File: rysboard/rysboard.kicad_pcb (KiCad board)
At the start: 4 copper layers, 56 x 65 mm, 151 parts, among them J1 RPi4, J10 ToF1, J11 ToF2, J12 ToF3, J13 ToF4, J15 ToF5, J16 ToF6, J19 Fan_Connector, J2 Motor L, J20 Power_SW, J22 CH1_T, J23 CH2_T, J3 Motor R, J4 Cell3, J5 Cell2, J6 Cell1, J7 Conn_01x02, J9 IMU, Q1 DMP3036SSD-13, Q13 SI7997DP-T1-GE3, Q14 DMP2075UFDB-7-alt, Q2 DMP2075UFDB, Q3 NST847BDP6T5G, Q4 NST847BDP6T5G, Q5 DMP3036SSD-13, Q6 Si7938DP-T1-GE3, Q7 NST847BDP6T5G, Q9 Si7938DP-T1-GE3, U1 L6470, U2 L6470, U3 ST1S10, U4 STM32G031K8Ux, U5 74HC2G00, U6 AP7381-33SA-7, U7 LM74700, U8 LM74700, U9 INA181

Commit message: Bom finished pcb cleanup started
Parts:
- removed D10, D11, D12: TESDU5V0, Diode_SMD:D_0603_1608Metric_Pad1.05x0.95mm_HandSolder
- removed D14, D3: TSZU52C10 RG, Diode_SMD:D_0603_1608Metric
- removed D16: PTVS30VS1UR,115, Diode_SMD:D_SOD-123
- removed D7: LED, LED_SMD:LED_0805_2012Metric
- removed Q13: SI7997DP-T1-GE3, Package_SO:PowerPAK_SO-8_Dual
- removed Q14: DMP2075UFDB-7-alt, SamacSys_Parts:DMP2075UFDB7
- removed U7, U8: LM74700, Package_TO_SOT_SMD:SOT-23-6
- added D4: SZ1SMA15CAT3G, Diode_SMD:D_SMA_Handsoldering, F.Cu at (183.7, 89.7)
- added IC1: LM74801QDRRRQ1, LM74801QDRRRQ1, F.Cu at (165.7, 86.6)
- added IC2: LM74801QDRRRQ1, LM74801QDRRRQ1, F.Cu at (181.9, 100.7)
- added Q10: AO3401A, Package_TO_SOT_SMD:SOT-23, F.Cu at (168.6, 104.5)
- added Q11: AO3401A, Package_TO_SOT_SMD:SOT-23, F.Cu at (156.8, 104.5)
- added R32: 100R, Resistor_SMD:R_0603_1608Metric, F.Cu at (187.2, 98.9)
- D13: value TSZU52C10 RG -> SZ1SMA15CAT3G; footprint Diode_SMD:D_0603_1608Metric -> Diode_SMD:D_SMA_Handsoldering
- F2: footprint Fuse:Fuse_2512_6332Metric -> Fuse:Fuse_1206_3216Metric
- J22, J23: footprint Connector_PinHeader_1.00mm:PinHeader_1x02_P1.00mm_Vertical -> Connector_PinHeader_1.27mm:PinHeader_1x02_P1.27mm_Vertical
- Q2: value DMP2075UFDB -> FDG6304P; footprint SamacSys_Parts:DMP2075UFDB7 -> SOT65P210X110-6N; moved to F.Cu
- R10: value 110KR -> 10KR
- R15: value 10KR -> 100R; moved to F.Cu
- R16: value 100R -> 110KR; moved to F.Cu
- R17: value 100R -> 10KR; moved to F.Cu
- R19: value 10K -> 100R; moved to F.Cu
- R22, R24: value 10KR -> 110KR
- R8: value 10k -> 110KR
- U3: footprint Package_SO:TI_SO-PowerPAD-8 -> Package_DFN_QFN:DFN-8-1EP_4x4mm_P0.8mm_EP2.3x3.24mm
- moved R16 88.2 mm to (171.3, 88.7), turned to 0 degrees
- moved Q4 87.8 mm to (180.0, 93.2)
- moved R23 83.0 mm to (171.3, 91.2), turned to 0 degrees
- moved R22 77.3 mm to (165.1, 97.3), turned to 0 degrees
- moved Q9 71.4 mm to (171.5, 84.0), turned to 270 degrees
- moved R15 68.4 mm to (164.8, 94.8), turned to 0 degrees
- moved R17 67.8 mm to (161.1, 97.3), turned to 0 degrees
- moved Q2 65.0 mm to (156.9, 95.8)
- moved R19 56.9 mm to (168.8, 94.8), turned to 0 degrees
- moved C18 0.48 mm to (94.9, 107.9)
- moved R14 0.46 mm to (94.9, 111.0)
- moved U3 0.42 mm to (99.3, 109.6)
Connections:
- C28 pad 1: /Power Supply/Battery_Balancing/V_BAT_AF_PROT- -> Net-(C28-Pad1)
- C28 pad 2: Net-(C28-Pad2) -> +BATT
- C29 pad 2: +BATT -> +12V
- C31 pad 1: /Power Supply/Batterry_Charging_Powes_Spply/VCAP -> +BATT
- C31 pad 2: GND -> Net-(C31-Pad2)
- F1 pad 1: Net-(D10-Pad1) -> Net-(F1-Pad1)
- J20 pad 1: Net-(J20-Pad1) -> /Power Supply/Battery_Balancing/V_BAT_AF_PROT-
- J20 pad 2: /Power Supply/Battery_Balancing/V_BAT_AF_PROT+ -> Net-(F1-Pad1)
- J4 pad 1: Net-(D12-Pad2) -> Net-(F1-Pad2)
- J6 pad 2: Net-(F1-Pad2) -> /Power Supply/Battery_Balancing/V_BAT_AF_PROT+
- Q1 pad 3: +BATT -> (no net)
- Q1 pad 4: Net-(D3-Pad2) -> (no net)
- Q1 pad 5: +12V -> (no net)
- Q1 pad 6: +12V -> (no net)
- Q2 pad 1: MCU_3.3V -> Net-(Q2-Pad1)
- Q2 pad 3: /Sensors/TOF_5V -> Net-(J4-Pad2)
- Q2 pad 4: +5V -> Net-(Q2-Pad4)
- Q2 pad 6: MCU_ANALOG_SENSOR_V -> Net-(J5-Pad2)
- Q4 pad 1: GND -> (no net)
- Q4 pad 2: Net-(Q4-Pad2) -> (no net)
- Q4 pad 6: Net-(D3-Pad2) -> (no net)
- Q7 pad 3: Net-(Q2-Pad5) -> Net-(Q11-Pad1)
- Q9 pad 1: /Power Supply/Battery_Balancing/V_BAT_AF_PROT- -> +12V
- Q9 pad 2: Net-(Q9-Pad2) -> Net-(IC1-Pad8)
- Q9 pad 5: Net-(D12-Pad2) -> +BATT
- R1 pad 1: +3V3 -> GND
- R10 pad 1: +BATT -> Net-(Q2-Pad2)
- R10 pad 2: Net-(D3-Pad2) -> /Power Supply/Battery_Balancing/V_BAT_AF_PROT-
- R15 pad 1: Net-(Q9-Pad2) -> Net-(Q2-Pad4)
- R15 pad 2: Net-(D11-Pad2) -> V_CELL1
- R16 pad 1: Net-(J5-Pad2) -> Net-(Q2-Pad5)
- R16 pad 2: Net-(D10-Pad2) -> Net-(J4-Pad2)
- R17 pad 1: Net-(J4-Pad2) -> Net-(Q2-Pad5)
- R17 pad 2: Net-(D11-Pad2) -> /Power Supply/Battery_Balancing/V_BAT_AF_PROT-
- R18 pad 1: Net-(J20-Pad1) -> Net-(IC1-Pad4)
- R19 pad 1: +BATT -> Net-(Q2-Pad1)
- R19 pad 2: Net-(D7-Pad2) -> V_CELL2
- R22 pad 1: V_CELL2 -> +BATT
- R22 pad 2: Net-(Q13-Pad2) -> Net-(IC1-Pad5)
- R23 pad 1: V_CELL1 -> Net-(R23-Pad1)
- R23 pad 2: Net-(Q14-Pad5) -> Net-(IC1-Pad5)
- R24 pad 2: Net-(Q14-Pad2) -> /ENABLE_RAIL_12V
- R51 pad 2: Net-(Q2-Pad5) -> Net-(Q11-Pad1)
- R64 pad 1: Net-(Q2-Pad2) -> Net-(Q10-Pad1)
- R66 pad 2: Net-(Q2-Pad2) -> Net-(Q10-Pad1)
- R8 pad 1: /ENABLE_RAIL_12V -> Net-(Q2-Pad2)
- R8 pad 2: Net-(Q4-Pad2) -> Net-(J5-Pad2)
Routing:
- net Net-(Q4-Pad2): track 46.2 -> 0.00 mm, vias 2 -> 0
- net Net-(J20-Pad1): track 43.0 -> 0.00 mm, vias 1 -> 0
- net GND: track 348.3 -> 308.5 mm
- net Net-(Q2-Pad2): track 34.9 -> 0.00 mm, vias 2 -> 0
- net Net-(Q10-Pad1): track 0.00 -> 34.9 mm, vias 0 -> 2
- net Net-(J5-Pad2): track 12.6 -> 47.4 mm
- net /Power Supply/Battery_Balancing/V_BAT_AF_PROT-: track 66.3 -> 35.3 mm, vias 2 -> 3
- net Net-(Q2-Pad5): track 30.0 -> 0.00 mm, vias 2 -> 0
- net Net-(Q11-Pad1): track 0.00 -> 30.0 mm, vias 0 -> 2
- net Net-(D12-Pad2): track 15.8 -> 0.00 mm
- net /Power Supply/Battery_Balancing/V_BAT_AF_PROT+: track 23.1 -> 7.83 mm
- net Net-(J4-Pad2): track 13.6 -> 0.93 mm, vias 1 -> 0
- net Net-(D3-Pad2): track 10.8 -> 0.00 mm, vias 2 -> 0
- net Net-(D11-Pad2): track 21.6 -> 11.9 mm, vias 3 -> 1
- net /Power Supply/SW: track 9.66 -> 0.85 mm
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
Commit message: bom + excel ready
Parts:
- added D10: TSZU52C13 RGG, Diode_SMD:D_0603_1608Metric, F.Cu at (191.7, 94.1)
- added D3: TSZU52C13 RGG, Diode_SMD:D_0603_1608Metric, F.Cu at (171.9, 71.8)
- added D7: CD0603-Z3, Diode_SMD:D_0603_1608Metric, F.Cu at (158.0, 70.9)
- added R33: 10k1%, Resistor_SMD:R_0603_1608Metric, F.Cu at (158.0, 78.9)
- added R34: 10k1%, Resistor_SMD:R_0603_1608Metric, F.Cu at (162.0, 70.8)
- added R35: 2.8KR, Resistor_SMD:R_0603_1608Metric, F.Cu at (162.0, 73.3)
- C24, C25, C26, C28, C31, C45: value 0.1uF -> 100n
- C27, C34: value 10uF -> 10u
- C32: value 0,1uF -> 100n
- C33: value 0.1uF10% -> 100n
- D4: value SZ1SMA15CAT3G -> TSZU52C13 RGG; footprint Diode_SMD:D_SMA_Handsoldering -> Diode_SMD:D_0603_1608Metric
- IC1, IC2: footprint LM74801QDRRRQ1 -> SamacSys_Parts:LM74801QDRRRQ1
- Q2: footprint SOT65P210X110-6N -> SamacSys_Parts:SOT65P210X110-6N
- R10, R17, R23, R31, R40, R51, R55, R56, R59, R61, R62, R64, R68, R7, R70, R71: value 10KR -> 10k1%
- R11: value 10k -> 10k1%
- moved D4 5.99 mm to (187.7, 94.1)
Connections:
- D4 pad 1: +12V -> Net-(D3-Pad2)
- D4 pad 2: Net-(D4-Pad2) -> Net-(D10-Pad2)
- IC1 pad 6: /ENABLE_RAIL_12V -> Net-(IC1-Pad6)
- Q1 pad 2: Net-(D4-Pad2) -> Net-(Q1-Pad2)
- Q4 pad 3: Net-(D4-Pad2) -> Net-(Q1-Pad2)
- R12 pad 2: Net-(D4-Pad2) -> Net-(Q1-Pad2)
- R23 pad 1: Net-(R23-Pad1) -> /Power Supply/Battery_Balancing/V_BAT_AF_PROT-
- R24 pad 2: /ENABLE_RAIL_12V -> Net-(IC1-Pad6)
- U4 pad 13: Net-(U4-Pad13) -> /V_AUX
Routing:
- net Net-(Q1-Pad2): track 0.00 -> 8.28 mm, vias 0 -> 1
- net Net-(D4-Pad2): track 8.28 -> 0.00 mm, vias 1 -> 0
- net Net-(IC1-Pad6): track 0.00 -> 4.92 mm
- net /ENABLE_RAIL_12V: track 7.88 -> 2.96 mm

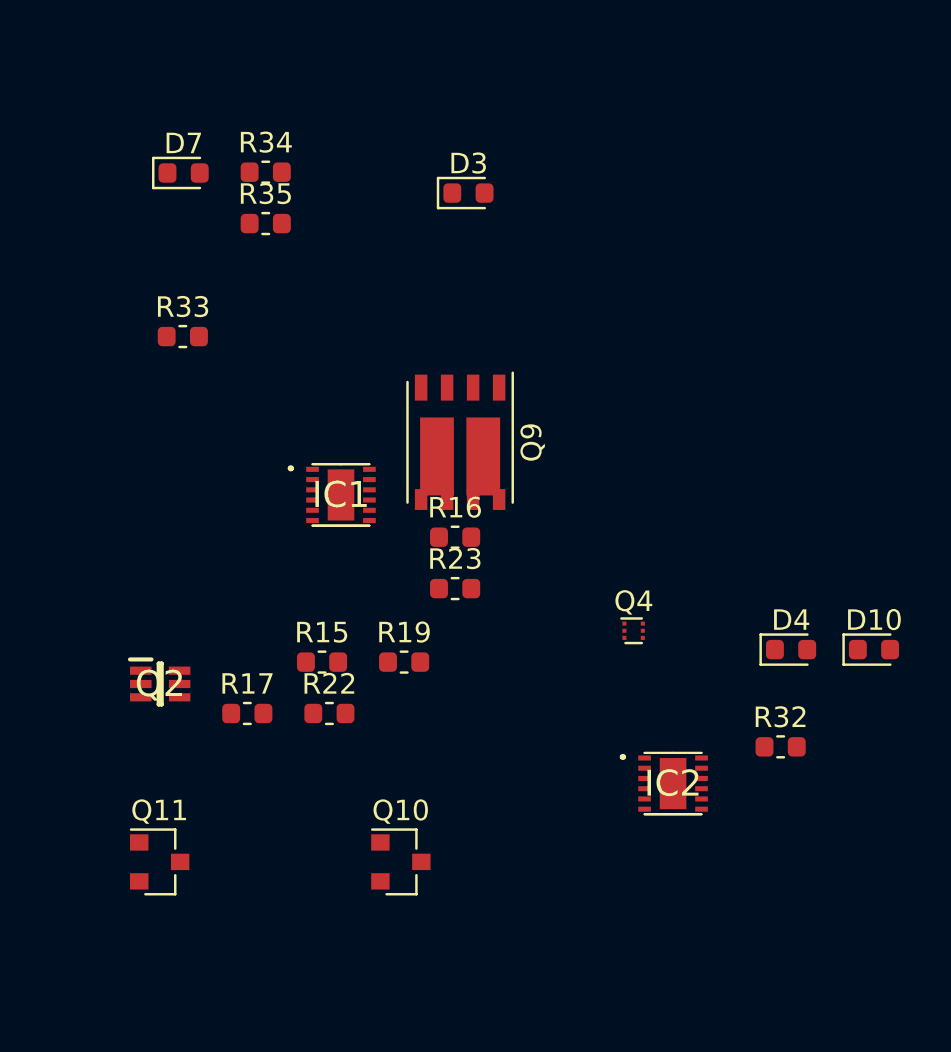
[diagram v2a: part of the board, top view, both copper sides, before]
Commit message: Step down L7986A test board
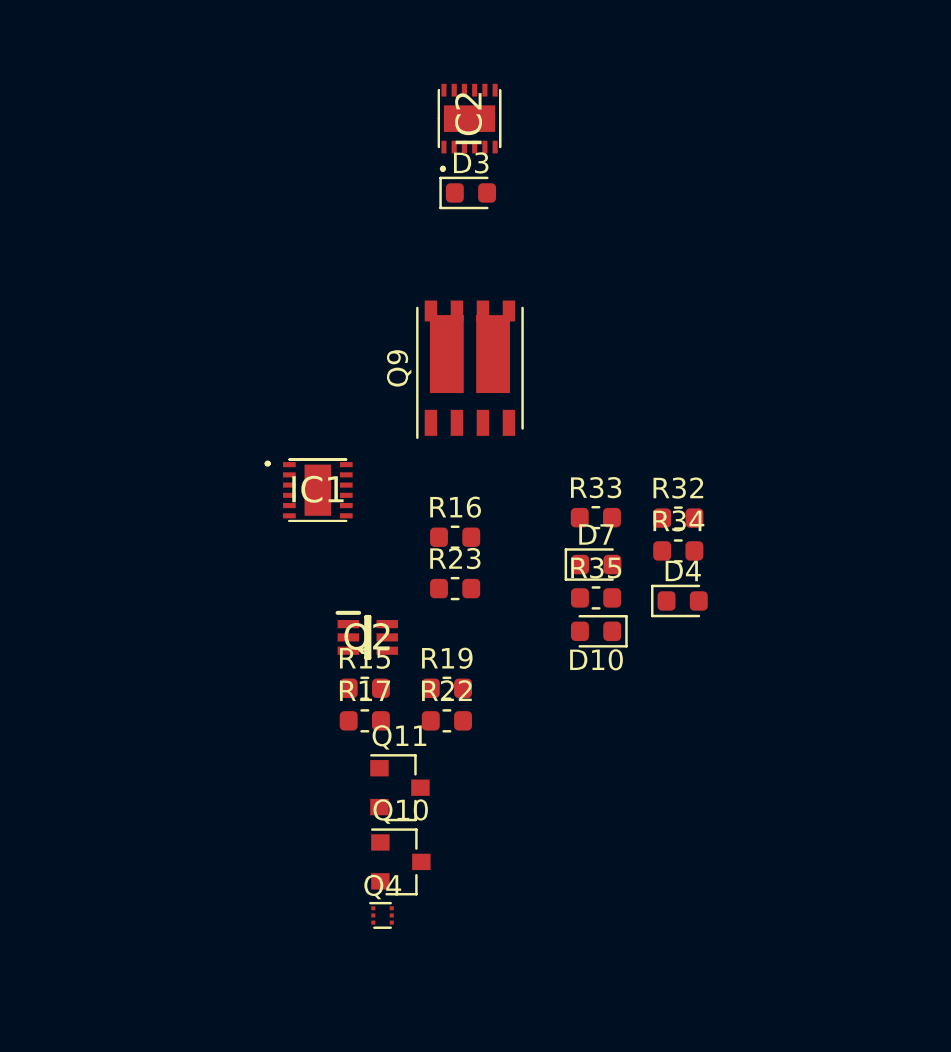
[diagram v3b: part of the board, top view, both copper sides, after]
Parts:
- moved IC2 34.0 mm to (172.0, 68.2), turned to 90 degrees
- moved D7 27.8 mm to (178.2, 90.0)
- moved R34 27.4 mm to (182.2, 89.3)
- moved R35 24.4 mm to (178.2, 91.6)
- moved R33 22.0 mm to (178.1, 87.7)
- moved Q4 18.5 mm to (167.7, 107.1)
- moved D10 13.6 mm to (178.2, 93.2), turned to 180 degrees
- moved Q11 12.3 mm to (168.6, 100.9)
- moved R32 12.2 mm to (182.2, 87.7)
- moved Q2 10.4 mm to (167.0, 93.5)
- moved D4 5.80 mm to (182.4, 91.8)
- moved R22 5.75 mm to (170.9, 97.6)
- moved R17 5.75 mm to (166.9, 97.6)
- moved Q9 3.65 mm to (172.0, 80.4), turned to 90 degrees
- moved R19 2.45 mm to (170.9, 96.0)
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
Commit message: cleanup  done
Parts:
- removed D13: SZ1SMA15CAT3G, Diode_SMD:D_SMA_Handsoldering
- added R36: 1k, Resistor_SMD:R_0603_1608Metric, F.Cu at (152.2, 70.8)
- C17, C29, C32, Q3, Q5, Q7, R10, R12, R18, R51, R52, R62, R66, R69, R7, R8, TH2: moved to F.Cu
- F1: moved to B.Cu
- Q1: value DMP3036SSD-13 -> PMV28XPEAR; footprint Package_SO:SO-8_3.9x4.9mm_P1.27mm -> Package_TO_SOT_SMD:SOT-23
- Q10, Q11: value AO3401A -> PMV28XPEAR
- R71: value 10k1% -> 10KR; moved to F.Cu
- U3: footprint Package_DFN_QFN:DFN-8-1EP_4x4mm_P0.8mm_EP2.3x3.24mm -> Package_SO:TI_SO-PowerPAD-8
- moved R51 88.7 mm to (175.5, 133.3), turned to 0 degrees
- moved R12 86.6 mm to (184.7, 112.2), turned to 0 degrees
- moved R16 83.4 mm to (101.7, 134.8)
- moved R70 83.2 mm to (166.7, 133.3), turned to 0 degrees
- moved R66 81.1 mm to (162.7, 135.8)
- moved R15 80.8 mm to (98.0, 138.3), turned to 180 degrees
- moved Q2 78.9 mm to (101.8, 138.0), turned to 180 degrees
- moved R19 78.1 mm to (105.3, 138.6)
- moved R17 78.0 mm to (98.3, 134.8), turned to 180 degrees
- moved R18 77.8 mm to (164.2, 114.8), turned to 0 degrees
- moved C32 76.2 mm to (162.7, 133.3)
- moved C17 75.9 mm to (185.5, 109.3)
- moved R69 73.0 mm to (176.3, 121.0), turned to 0 degrees
- moved Q5 70.4 mm to (178.5, 110.9), turned to 0 degrees
- moved R24 70.0 mm to (164.4, 112.2), turned to 0 degrees
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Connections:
- Q1 pad 1: +12V -> Net-(Q1-Pad1)
- Q1 pad 2: Net-(Q1-Pad2) -> +12V
- Q1 pad 3: (no net) -> /Power Supply/Fan_12V
- Q4 pad 3: Net-(Q1-Pad2) -> Net-(Q4-Pad3)
- Q5 pad 2: Net-(D13-Pad2) -> Net-(Q4-Pad3)
- Q5 pad 7: /Power Supply/Fan_12V -> /Power Supply/ST_Down_12V
- Q5 pad 8: /Power Supply/Fan_12V -> /Power Supply/ST_Down_12V
- Q7 pad 6: Net-(D13-Pad2) -> Net-(Q7-Pad6)
- R12 pad 2: Net-(Q1-Pad2) -> Net-(Q4-Pad3)
- R7 pad 2: Net-(D13-Pad2) -> Net-(Q1-Pad1)
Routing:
- net GND: track 308.5 -> 173.7 mm, vias 28 -> 3
- net +BATT: track 111.0 -> 21.7 mm, vias 8 -> 1
- net +12V: track 75.3 -> 0.00 mm, vias 17 -> 0
- net /Power Supply/ST_Down_12V: track 69.4 -> 0.75 mm, vias 6 -> 0
- net Net-(J5-Pad2): track 47.4 -> 0.30 mm, vias 1 -> 0
- net MCU_3.3V: track 91.9 -> 45.8 mm, vias 3 -> 1
- net MCU_ANALOG_SENSOR_V: track 51.4 -> 14.9 mm, vias 6 -> 4
- net Net-(Q10-Pad1): track 34.9 -> 1.11 mm, vias 2 -> 0
- net Net-(Q11-Pad1): track 30.0 -> 0.00 mm, vias 2 -> 0
- net /BOARD_TEMP_PROBE_1: track 62.0 -> 36.6 mm
- net Net-(Q4-Pad5): track 45.4 -> 21.0 mm
- net /VOLTAGE_PROBE_5V: track 95.7 -> 72.4 mm, vias 2 -> 1
- net Net-(D10-Pad2): track 22.7 -> 0.00 mm, vias 1 -> 0
- net /VBAT_2: track 80.3 -> 60.4 mm, vias 2 -> 1
- net /Power Supply/Fan_12V: track 19.7 -> 0.00 mm, vias 1 -> 0
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
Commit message: bat protection done
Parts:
- C27, C28, IC1, Q2, Q9, R10, R15, R16, R17, R18, R19, R22, R23, R24, R33, R8: moved to B.Cu
- moved Q9 89.0 mm to (89.0, 112.7)
- moved R33 83.3 mm to (100.8, 118.8)
- moved C27 78.9 mm to (86.8, 118.0)
- moved C28 75.6 mm to (92.8, 113.0), turned to 90 degrees
- moved R23 75.1 mm to (100.8, 117.3), turned to 180 degrees
- moved IC1 73.8 mm to (96.5, 114.8), turned to 180 degrees
- moved R22 72.3 mm to (100.8, 115.8), turned to 180 degrees
- moved R24 64.1 mm to (100.8, 120.3), turned to 180 degrees
- moved R18 63.3 mm to (100.8, 114.2)
- moved C29 25.5 mm to (181.6, 102.2)
- moved R19 21.8 mm to (97.3, 118.4)
- moved Q2 20.6 mm to (94.0, 119.0)
- moved R15 20.1 mm to (90.7, 119.6)
- moved R8 19.5 mm to (91.8, 123.8), turned to 270 degrees
- moved R10 15.1 mm to (90.2, 123.8), turned to 270 degrees
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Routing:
- net Net-(C15-Pad1): track 73.1 -> 27.2 mm
- net +BATT: track 21.7 -> 63.4 mm, vias 1 -> 3
- net /Power Supply/Battery_Balancing/V_BAT_AF_PROT+: track 0.20 -> 24.1 mm, vias 0 -> 2
- net +12V: track 0.00 -> 21.7 mm, vias 0 -> 3
- net Net-(J5-Pad2): track 0.30 -> 19.4 mm
- net Net-(J4-Pad2): track 0.00 -> 17.3 mm
- net Net-(IC1-Pad1): track 0.00 -> 14.9 mm, vias 0 -> 2
- net Net-(Q2-Pad5): track 0.00 -> 13.3 mm, vias 0 -> 2
- net Net-(Q2-Pad2): track 0.00 -> 8.66 mm, vias 0 -> 2
- net Net-(IC1-Pad8): track 0.00 -> 7.91 mm
- net Net-(IC1-Pad6): track 0.00 -> 5.74 mm
- net /SWDIO: track 58.7 -> 64.0 mm
- net /SWCLK: track 63.6 -> 68.5 mm
- net /MCU_RST: track 61.3 -> 66.2 mm
- net Net-(F1-Pad1): track 0.00 -> 4.09 mm
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- added copper zone on B.Cu, net +BATT
- added copper zone on B.Cu, net /Power Supply/Battery_Balancing/V_BAT_AF_PROT-

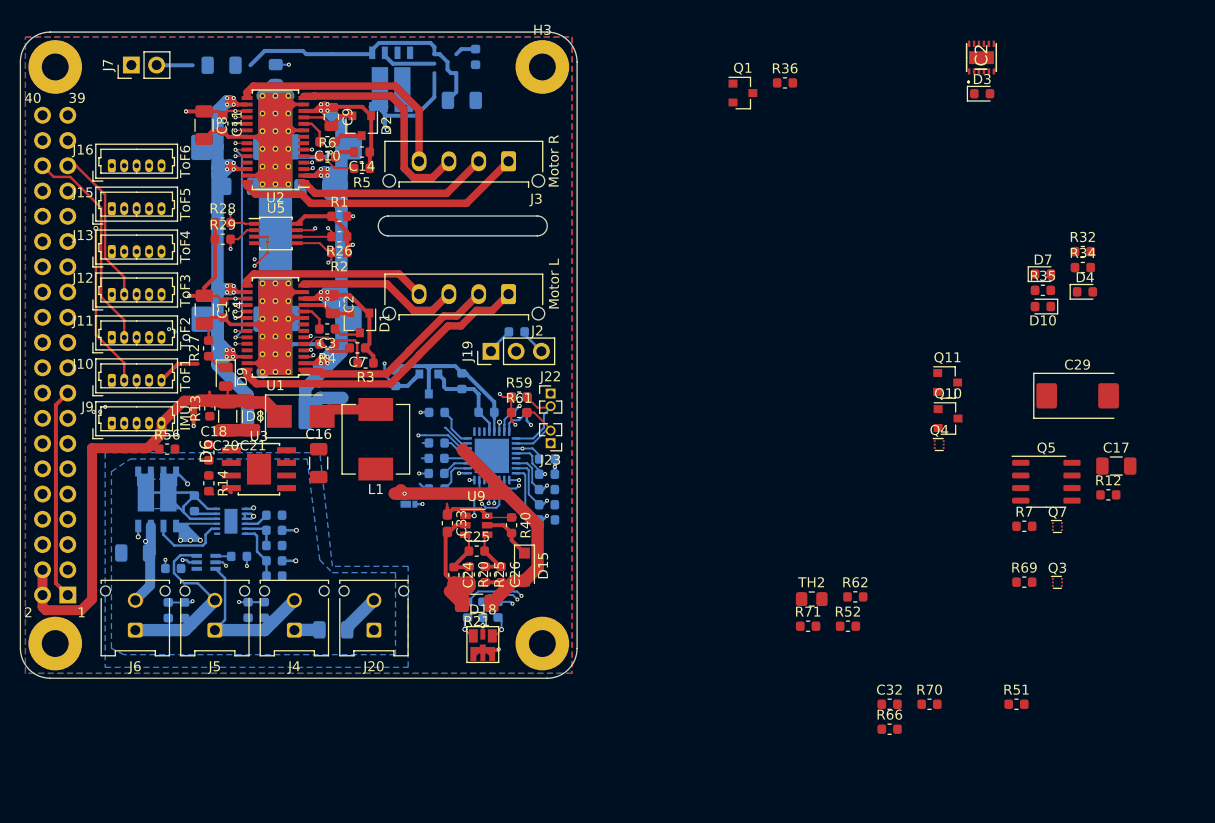
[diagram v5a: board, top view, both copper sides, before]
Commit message: vin protection added
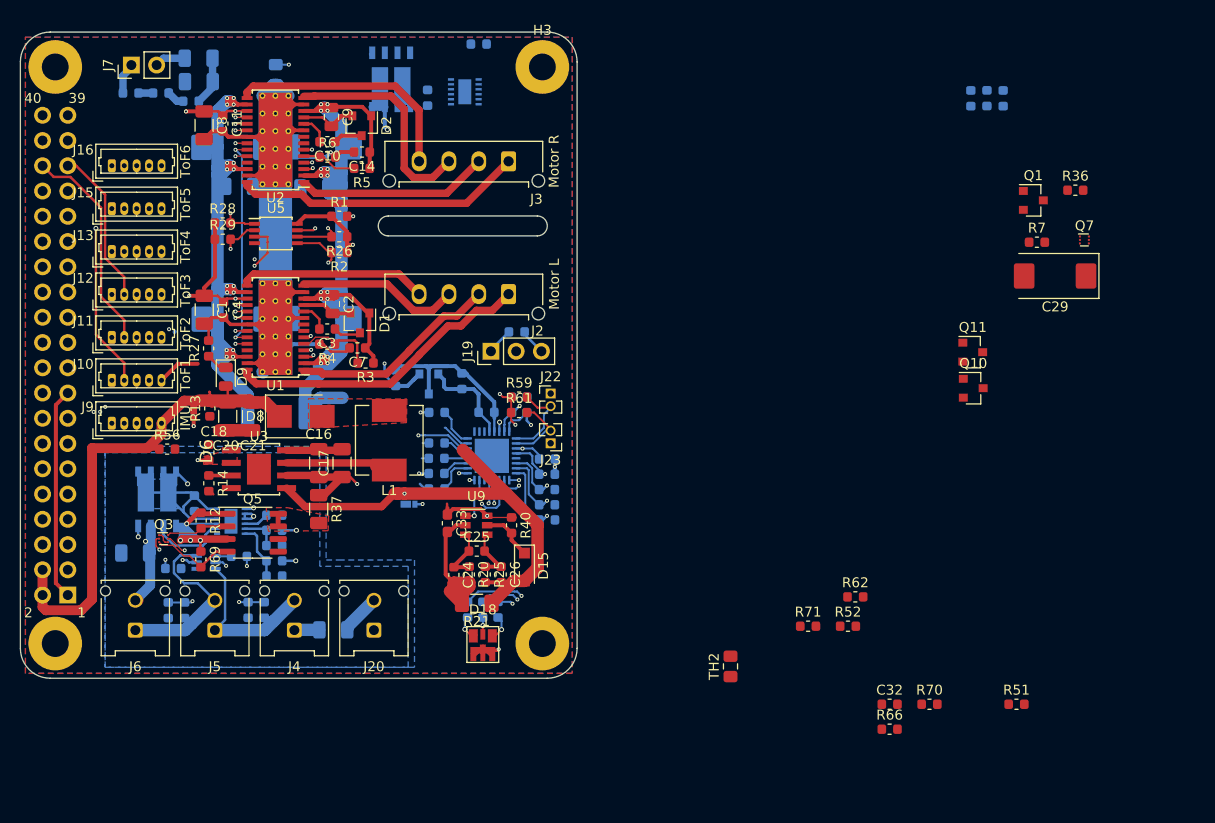
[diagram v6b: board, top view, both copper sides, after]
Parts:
- removed the Q3 at (179.6, 121.0)
- added R37: 0R, Resistor_SMD:R_1206_3216Metric, F.Cu at (105.3, 113.6)
- D10, D3, D4, D7, IC2, R32, R34, R35: moved to B.Cu
- moved D4 95.1 mm to (89.4, 71.8), turned to 180 degrees
- moved D10 94.2 mm to (86.4, 71.8), turned to 0 degrees
- moved R12 91.3 mm to (93.5, 114.8), turned to 270 degrees
- moved R69 82.9 mm to (93.5, 118.7), turned to 270 degrees
- moved Q5 80.0 mm to (98.7, 116.0)
- moved D3 79.6 mm to (92.5, 72.6), turned to 180 degrees
- moved Q3 78.6 mm to (89.7, 116.6)
- moved C17 77.9 mm to (107.7, 109.0), turned to 90 degrees
- moved R32 64.3 mm to (121.4, 66.8)
- moved IC2 52.1 mm to (120.0, 71.7), turned to 0 degrees
- moved Q1 31.1 mm to (177.2, 82.6)
- moved R36 31.1 mm to (181.4, 81.6)
- moved Q7 29.0 mm to (182.3, 86.5)
- moved R7 28.6 mm to (177.6, 86.8)
- moved C34 26.5 mm to (93.2, 70.6), turned to 180 degrees
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- renumbered Q4 to Q3
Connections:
- Q3 pad 1: (no net) -> GND
- Q3 pad 2: (no net) -> Net-(Q3-Pad2)
- Q3 pad 3: Net-(Q4-Pad3) -> Net-(Q3-Pad3)
- Q3 pad 5: Net-(Q4-Pad5) -> Net-(Q3-Pad5)
- Q3 pad 6: (no net) -> Net-(Q3-Pad6)
- Q5 pad 2: Net-(Q4-Pad3) -> Net-(Q3-Pad6)
- Q5 pad 7: /Power Supply/ST_Down_12V -> Net-(Q5-Pad7)
- Q5 pad 8: /Power Supply/ST_Down_12V -> Net-(Q5-Pad7)
- R11 pad 2: Net-(Q4-Pad5) -> Net-(Q3-Pad2)
- R12 pad 2: Net-(Q4-Pad3) -> Net-(Q3-Pad6)
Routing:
- net /Power Supply/ST_Down_12V: track 0.75 -> 30.1 mm, vias 0 -> 2
- net Net-(Q3-Pad2): track 0.00 -> 22.5 mm, vias 0 -> 2
- net Net-(C34-Pad1): track 27.3 -> 5.42 mm
- net GND: track 173.7 -> 195.4 mm
- net Net-(Q4-Pad5): track 21.0 -> 0.00 mm, vias 1 -> 0
- net +BATT: track 63.4 -> 52.4 mm
- net +12V: track 21.7 -> 32.1 mm, vias 3 -> 4
- net /Power Supply/SW: track 0.85 -> 10.9 mm
- net Net-(Q3-Pad3): track 0.00 -> 8.53 mm
- net Net-(Q3-Pad6): track 0.00 -> 6.29 mm
- net Net-(IC2-Pad1): track 5.62 -> 0.30 mm
- net Net-(D8-Pad2): track 5.69 -> 0.99 mm
- net /Power Supply/FB: track 0.06 -> 2.32 mm
- net Net-(Q3-Pad5): track 1.03 -> 3.19 mm, vias 1 -> 2
- net Net-(D3-Pad2): track 0.00 -> 1.92 mm
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- added copper zone on F.Cu, net /Power Supply/ST_Down_12V
- added copper zone on F.Cu, net Net-(D8-Pad2)
- added copper zone on F.Cu, net Net-(Q5-Pad7)
